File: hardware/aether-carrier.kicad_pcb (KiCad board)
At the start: 2 copper layers, 100 x 90 mm, 34 parts, among them J1 DevKitC-1 socket J1, J10 REC LED, J2 DevKitC-1 socket J3, J3 5V INPUT, J4 LCD, J5 MIC 3V3, J6 AMP 5V, J7 RING 5V, J8 PTT, J9 PAGE, Q1 AO3401A, U1 SN74AHCT1G125

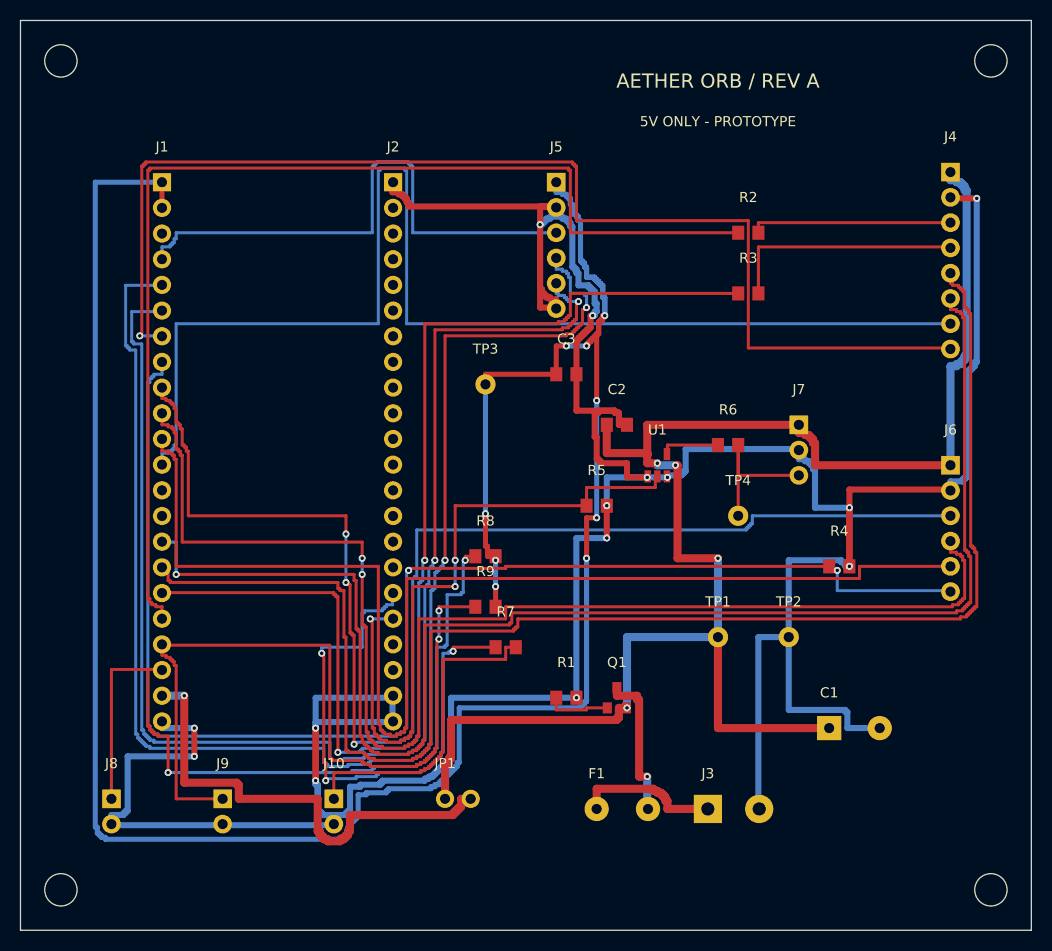
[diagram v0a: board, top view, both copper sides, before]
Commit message: engineering: Rev B zero-interference CAD, sealed STL meshes and carrier corrections
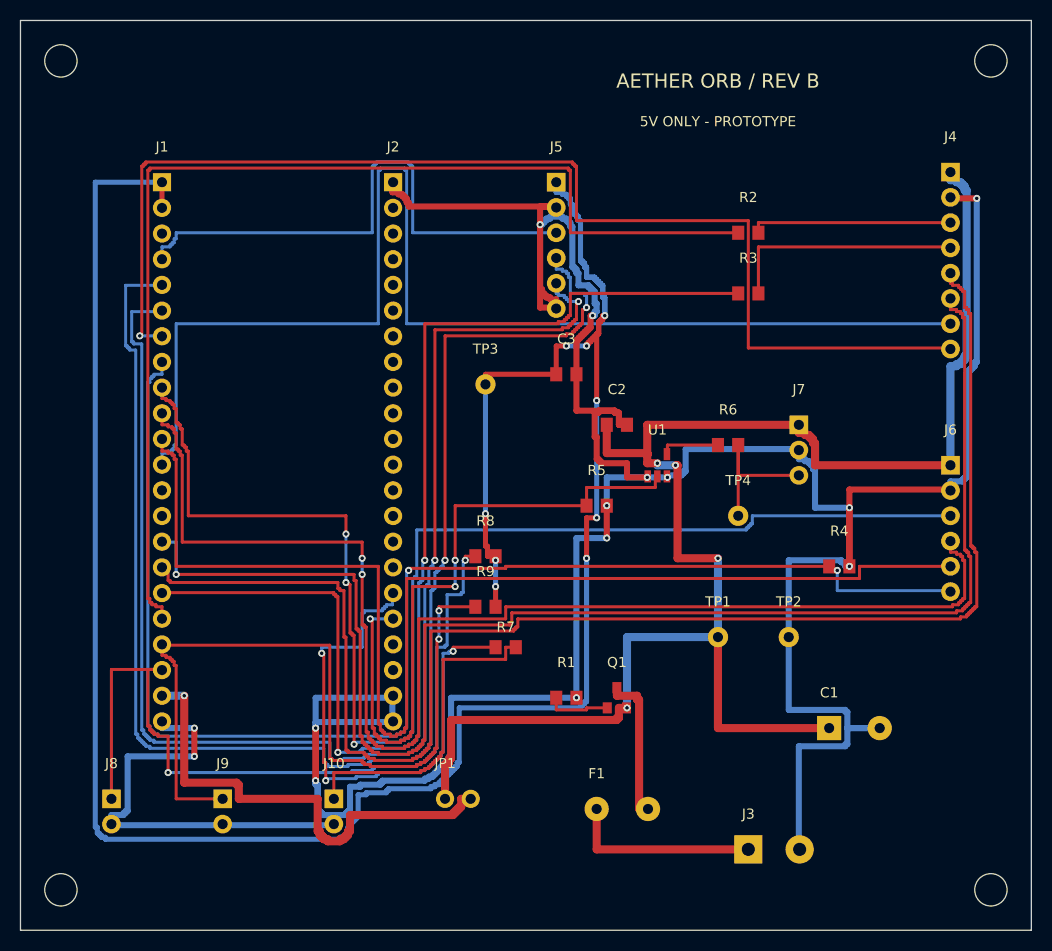
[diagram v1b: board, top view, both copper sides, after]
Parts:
- C1: footprint Aether:CP_Radial_D10_P5 -> Aether:CP_Radial_D10_P5_C1
- C2: footprint Aether:C_0805_2012Metric -> Aether:C_0805_2012Metric_C2
- C3: footprint Aether:C_0805_2012Metric -> Aether:C_0805_2012Metric_C3
- F1: footprint Aether:PTC_P5.08 -> Aether:PTC_P5.08_F1
- J1: footprint Aether:Socket_1x22_P2.54 -> Aether:Socket_1x22_P2.54_J1
- J10: footprint Aether:XH_1x02_P2.50 -> Aether:XH_1x02_P2.50_J10
- J2: footprint Aether:Socket_1x22_P2.54 -> Aether:Socket_1x22_P2.54_J2
- J3: footprint Aether:Terminal_1x02_P5.08 -> Aether:Terminal_1x02_P5.08_J3
- J4: footprint Aether:XH_1x08_P2.50 -> Aether:XH_1x08_P2.50_J4
- J5: footprint Aether:XH_1x06_P2.50 -> Aether:XH_1x06_P2.50_J5
- J6: footprint Aether:XH_1x06_P2.50 -> Aether:XH_1x06_P2.50_J6
- J7: footprint Aether:XH_1x03_P2.50 -> Aether:XH_1x03_P2.50_J7
- J8: footprint Aether:XH_1x02_P2.50 -> Aether:XH_1x02_P2.50_J8
- J9: footprint Aether:XH_1x02_P2.50 -> Aether:XH_1x02_P2.50_J9
- JP1: footprint Aether:PinHeader_1x02_P2.54 -> Aether:PinHeader_1x02_P2.54_JP1
- Q1: footprint Aether:SOT-23 -> Aether:SOT-23_Q1
- R1: footprint Aether:R_0805_2012Metric -> Aether:R_0805_2012Metric_R1
- R2: footprint Aether:R_0805_2012Metric -> Aether:R_0805_2012Metric_R2
- R3: footprint Aether:R_0805_2012Metric -> Aether:R_0805_2012Metric_R3
- R4: footprint Aether:R_0805_2012Metric -> Aether:R_0805_2012Metric_R4
- R5: footprint Aether:R_0805_2012Metric -> Aether:R_0805_2012Metric_R5
- R6: footprint Aether:R_0805_2012Metric -> Aether:R_0805_2012Metric_R6
- R7: footprint Aether:R_0805_2012Metric -> Aether:R_0805_2012Metric_R7
- R8: footprint Aether:R_0805_2012Metric -> Aether:R_0805_2012Metric_R8
- R9: footprint Aether:R_0805_2012Metric -> Aether:R_0805_2012Metric_R9
- TP1: footprint Aether:TestPoint_THT_D2 -> Aether:TestPoint_THT_D2_TP1
- TP2: footprint Aether:TestPoint_THT_D2 -> Aether:TestPoint_THT_D2_TP2
- TP3: footprint Aether:TestPoint_THT_D2 -> Aether:TestPoint_THT_D2_TP3
- TP4: footprint Aether:TestPoint_THT_D2 -> Aether:TestPoint_THT_D2_TP4
- U1: footprint Aether:SOT-23-5 -> Aether:SOT-23-5_U1
- moved J3 5.66 mm to (72.0, 82.0)
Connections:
- J1 pad 13: NC_GPIO3 -> unconnected-(J1-NC_GPIO3-Pad13)
- J1 pad 14: NC_GPIO46 -> unconnected-(J1-NC_GPIO46-Pad14)
- J1 pad 3: NC_EN -> unconnected-(J1-NC_EN-Pad3)
- J2 pad 10: NC_GPIO38 -> unconnected-(J2-NC_GPIO38-Pad10)
- J2 pad 11: NC_GPIO37 -> unconnected-(J2-NC_GPIO37-Pad11)
- J2 pad 12: NC_GPIO36 -> unconnected-(J2-NC_GPIO36-Pad12)
- J2 pad 13: NC_GPIO35 -> unconnected-(J2-NC_GPIO35-Pad13)
- J2 pad 14: NC_GPIO0 -> unconnected-(J2-NC_GPIO0-Pad14)
- J2 pad 15: NC_GPIO45 -> unconnected-(J2-NC_GPIO45-Pad15)
- J2 pad 16: NC_GPIO48 -> unconnected-(J2-NC_GPIO48-Pad16)
- J2 pad 19: NC_USB20 -> unconnected-(J2-NC_USB20-Pad19)
- J2 pad 2: NC_TX43 -> unconnected-(J2-NC_TX43-Pad2)
- J2 pad 20: NC_USB19 -> unconnected-(J2-NC_USB19-Pad20)
- J2 pad 3: NC_RX44 -> unconnected-(J2-NC_RX44-Pad3)
- J2 pad 4: NC_GPIO1 -> unconnected-(J2-NC_GPIO1-Pad4)
- J2 pad 5: NC_GPIO2 -> unconnected-(J2-NC_GPIO2-Pad5)
- J2 pad 6: NC_GPIO42 -> unconnected-(J2-NC_GPIO42-Pad6)
- J2 pad 7: NC_GPIO41 -> unconnected-(J2-NC_GPIO41-Pad7)
- J2 pad 8: NC_GPIO40 -> unconnected-(J2-NC_GPIO40-Pad8)
- J2 pad 9: NC_GPIO39 -> unconnected-(J2-NC_GPIO39-Pad9)
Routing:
- net VIN5: track 15.0 -> 19.0 mm
- net FUSED5: vias 1 -> 0
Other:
- board text added: "AETHER ORB / REV B"
- board text removed: "AETHER ORB / REV A"
